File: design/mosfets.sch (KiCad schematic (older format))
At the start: 15 parts, among them Q1 IRFS3006, Q2 IRFS3006, Q3 IRFS3006, Q4 IRFS3006, Q5 IRFS3006, Q6 IRFS3006

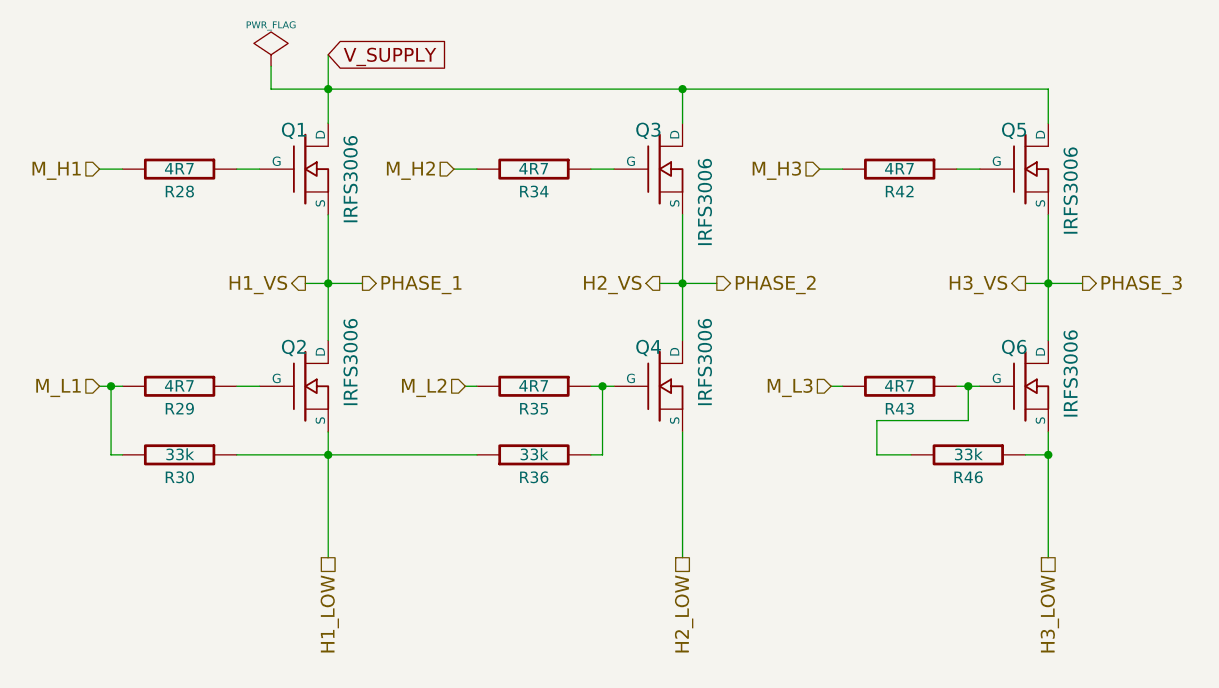
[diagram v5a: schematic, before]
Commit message: Moved nRST cap closer to the MCU pin, connected crystal GND pins to the actual GND plane. Added several vias to GND and VDD planes.
Signed-off-by: Marcos Chaparro <marcos@mrkindustries.com.ar>
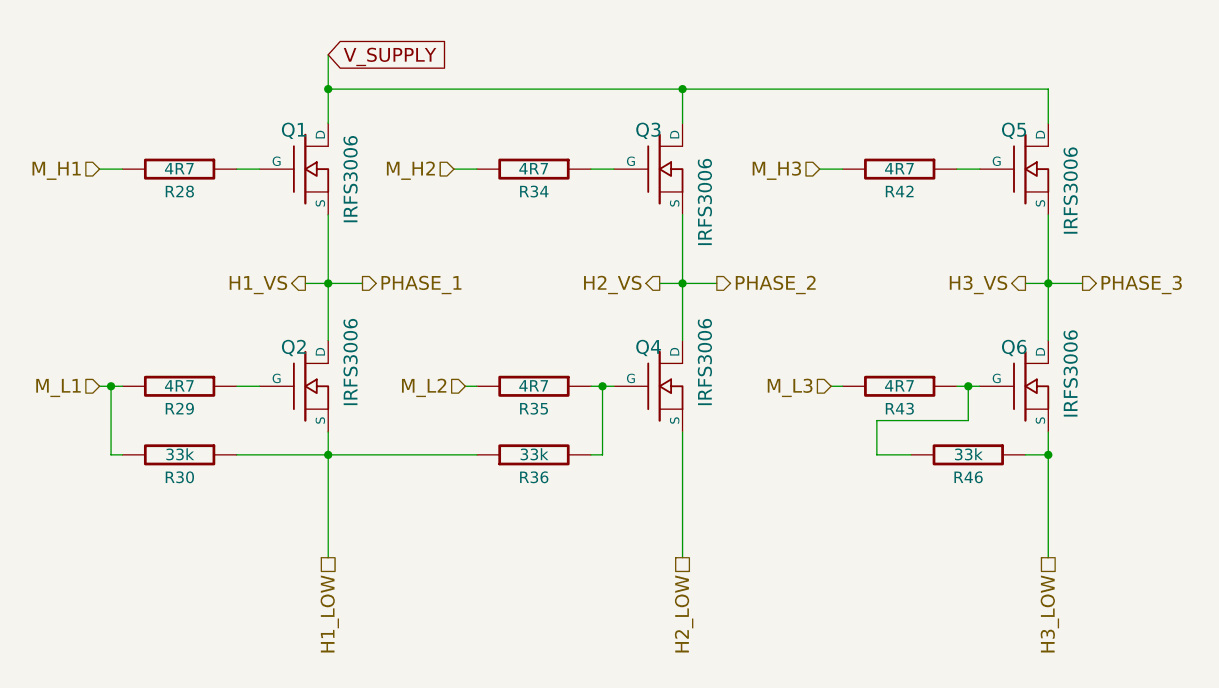
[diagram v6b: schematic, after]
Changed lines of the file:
@@
 	0    -1   -1   0
 $EndComp
-$Comp
-L PWR_FLAG #FLG024
-U 1 1 53F8E6AD
-P 4800 2350
-F 0 "#FLG024" H 4800 2445 30  0001 C CNN
-F 1 "PWR_FLAG" H 4800 2530 30  0000 C CNN
-F 2 "" H 4800 2350 60  0001 C CNN
-F 3 "" H 4800 2350 60  0001 C CNN
-	1    4800 2350
-	1    0    0    -1
-$EndComp
 Wire Wire Line
 	8100 4050 8200 4050
@@
 	4100 3750 4100 4050
 Wire Wire Line
-	4800 2450 8200 2450
+	5050 2450 8200 2450
 Wire Wire Line
 	7850 3750 7850 3900
@@
 Connection ~ 8200 4050
 Connection ~ 5050 4050
-Wire Wire Line
-	4800 2450 4800 2350
 Connection ~ 6250 3750
 Wire Wire Line
@@
 $Bitmap
 Pos 2050 6450
-Scale 1,000000
+Scale 1.000000
 Data
 89 50 4E 47 0D 0A 1A 0A 00 00 00 0D 49 48 44 52 00 00 03 8B 00 00 01 56 08 02 00 00 00 4F 4E 9F
@@
 F8 14 F0 0B 42 92 4F 42 07 35 54 00 00 00 00 00 00 7A 11 BC 6D 0C 00 00 00 00 00 F4 2D 50 43 05
 00 00 00 00 00 7D 0B D4 50 01 00 00 00 00 40 DF 02 35 54 00 00 00 00 00 D0 B7 FC 1F 55 28 1C 02
-4B 67 87 83 00 00 00 00 49 45 4E 44 AE 42 60 82 F0
+4B 67 87 83 00 00 00 00 49 45 4E 44 AE 42 60 82 90
 EndData
 $EndBitmap
 $Bitmap
 Pos 10150 5600
-Scale 1,000000
+Scale 1.000000
 Data
 89 50 4E 47 0D 0A 1A 0A 00 00 00 0D 49 48 44 52 00 00 02 72 00 00 02 1A 08 02 00 00 00 2B EB 37
@@
 00 00 00 41 83 58 05 00 00 08 1A C4 2A 00 00 40 D0 20 56 01 00 00 82 06 B1 0A 00 00 10 34 88 55
 00 00 80 A0 41 AC 02 00 00 04 CD FF 03 15 B2 0E 9E 1D 9F E2 F2 00 00 00 00 49 45 4E 44 AE 42 60
-82 47
+82 86
 EndData
 $EndBitmap
 $Bitmap
 Pos 6000 6850
-Scale 1,000000
+Scale 1.000000
 Data
 89 50 4E 47 0D 0A 1A 0A 00 00 00 0D 49 48 44 52 00 00 02 31 00 00 02 30 08 02 00 00 00 F8 51 AD
@@
 6D 12 06 83 C1 60 DA 0B D8 26 61 30 18 0C A6 BD 80 6D 12 06 83 C1 60 DA 0B D8 26 61 30 18 0C A6
 BD 80 6D 12 06 83 C1 60 DA 0B FF 03 68 C2 AC 3A A9 DC 0C E9 00 00 00 00 49 45 4E 44 AE 42 60 82
-98
+90
 EndData
 $EndBitmap
 $Bitmap
 Pos 4350 6700
-Scale 1,000000
+Scale 1.000000
 Data
 89 50 4E 47 0D 0A 1A 0A 00 00 00 0D 49 48 44 52 00 00 01 C1 00 00 01 D6 08 02 00 00 00 80 0A A5
@@
 $Bitmap
 Pos 2100 2150
-Scale 2,000000
+Scale 2.000000
 Data
 89 50 4E 47 0D 0A 1A 0A 00 00 00 0D 49 48 44 52 00 00 01 C2 00 00 01 99 08 02 00 00 00 95 33 A6
@@
 40 20 9C 12 44 46 09 04 02 E1 94 20 EE F7 67 02 30 C1 25 10 08 E7 25 24 1A 25 10 08 84 53 82 2C
 11 21 10 08 84 53 82 44 A3 04 02 81 70 4A 10 19 25 10 08 84 53 82 C8 28 81 40 20 9C 12 FF 1F 3E
-01 30 64 8D 18 65 07 00 00 00 00 49 45 4E 44 AE 42 60 82 18
+01 30 64 8D 18 65 07 00 00 00 00 49 45 4E 44 AE 42 60 82 85
 EndData
 $EndBitmap

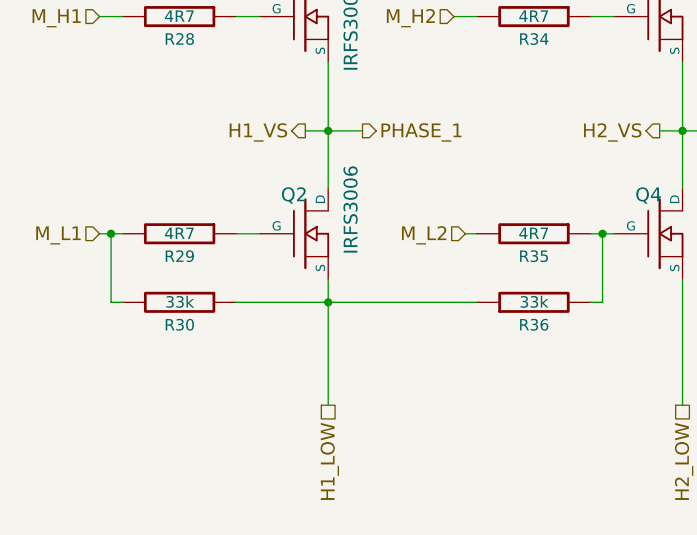
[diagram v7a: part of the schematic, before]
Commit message: Improved the path from one of the shunts to the amplifier
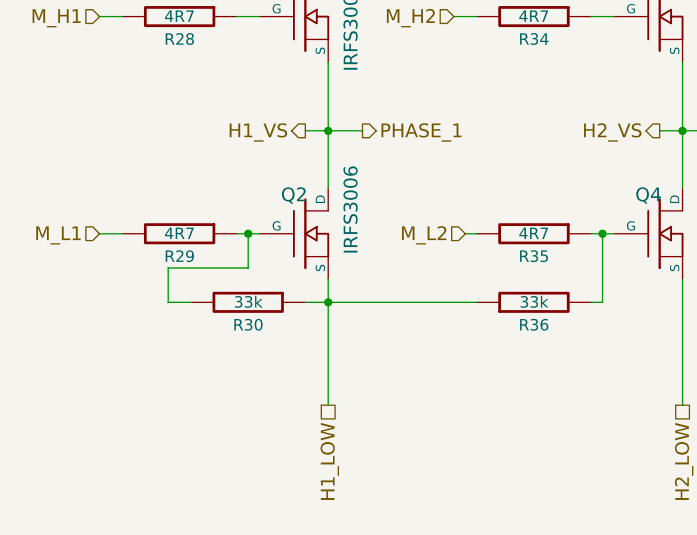
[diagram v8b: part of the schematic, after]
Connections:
- net M_L1: no longer R30.2
- net at Q2.G, R29.1: now also R30.2
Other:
- moved on the sheet: R30
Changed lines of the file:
@@
 LIBS:crf_1
 LIBS:BLDC_4-cache
-EELAYER 24 0
+EELAYER 25 0
 EELAYER END
 $Descr A4 11693 8268
@@
 L R R30
 U 1 1 53F8E612
-P 4400 4050
-F 0 "R30" V 4500 4050 50  0000 C CNN
-F 1 "33k" V 4400 4050 50  0000 C CNN
-F 2 "SMD_Packages:SMD-0603_r" H 4400 4050 60  0001 C CNN
-F 3 "" H 4400 4050 60  0001 C CNN
-	1    4400 4050
+P 4700 4050
+F 0 "R30" V 4800 4050 50  0000 C CNN
+F 1 "33k" V 4700 4050 50  0000 C CNN
+F 2 "SMD_Packages:SMD-0603_r" H 4700 4050 60  0001 C CNN
+F 3 "" H 4700 4050 60  0001 C CNN
+	1    4700 4050
 	0    1    1    0
 $EndComp
@@
 	8100 4050 8200 4050
 Wire Wire Line
-	4650 4050 5700 4050
+	4950 4050 5700 4050
 Wire Wire Line
 	7250 3750 7300 3750
@@
 	4050 2800 4150 2800
 Wire Wire Line
-	4100 3750 4100 4050
-Wire Wire Line
 	5050 2450 8200 2450
 Wire Wire Line
@@
 V_SUPPLY
 Wire Wire Line
-	4100 4050 4150 4050
-Wire Wire Line
 	6600 3950 6600 4500
-Connection ~ 4100 3750
 Text HLabel 4050 2800 0    60   Input ~ 0
 M_H1
@@
 F8 14 F0 0B 42 92 4F 42 07 35 54 00 00 00 00 00 00 7A 11 BC 6D 0C 00 00 00 00 00 F4 2D 50 43 05
 00 00 00 00 00 7D 0B D4 50 01 00 00 00 00 40 DF 02 35 54 00 00 00 00 00 D0 B7 FC 1F 55 28 1C 02
-4B 67 87 83 00 00 00 00 49 45 4E 44 AE 42 60 82 80
+4B 67 87 83 00 00 00 00 49 45 4E 44 AE 42 60 82 10
 EndData
 $EndBitmap
@@
 00 00 00 41 83 58 05 00 00 08 1A C4 2A 00 00 40 D0 20 56 01 00 00 82 06 B1 0A 00 00 10 34 88 55
 00 00 80 A0 41 AC 02 00 00 04 CD FF 03 15 B2 0E 9E 1D 9F E2 F2 00 00 00 00 49 45 4E 44 AE 42 60
-82 87
+82 D8
 EndData
 $EndBitmap
@@
 6D 12 06 83 C1 60 DA 0B D8 26 61 30 18 0C A6 BD 80 6D 12 06 83 C1 60 DA 0B D8 26 61 30 18 0C A6
 BD 80 6D 12 06 83 C1 60 DA 0B FF 03 68 C2 AC 3A A9 DC 0C E9 00 00 00 00 49 45 4E 44 AE 42 60 82
-98
+10
 EndData
 $EndBitmap
@@
 40 20 9C 12 44 46 09 04 02 E1 94 20 EE F7 67 02 30 C1 25 10 08 E7 25 24 1A 25 10 08 84 53 82 2C
 11 21 10 08 84 53 82 44 A3 04 02 81 70 4A 10 19 25 10 08 84 53 82 C8 28 81 40 20 9C 12 FF 1F 3E
-01 30 64 8D 18 65 07 00 00 00 00 49 45 4E 44 AE 42 60 82 79
+01 30 64 8D 18 65 07 00 00 00 00 49 45 4E 44 AE 42 60 82 0F
 EndData
 $EndBitmap
+Connection ~ 4700 3750
+Wire Wire Line
+	4700 3750 4700 3900
+Wire Wire Line
+	4700 3900 4350 3900
+Wire Wire Line
+	4350 3900 4350 4050
+Wire Wire Line
+	4350 4050 4450 4050
 $EndSCHEMATC
